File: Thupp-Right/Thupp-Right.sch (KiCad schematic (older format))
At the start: 42 parts

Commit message: aligned footprints relative to plate
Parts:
- MX19: footprint Kailh_Choc:KailhChoc-1U -> Kailh_Choc:KailhChoc-2U
- MX21: footprint Kailh_Choc:KailhChoc-1U -> Kailh_Choc:KailhChoc-1.5U
- MX4: footprint Kailh_Choc:KailhChoc-2U -> Kailh_Choc:KailhChoc-1U
- MX8: footprint Kailh_Choc:KailhChoc-1.5U -> Kailh_Choc:KailhChoc-1U
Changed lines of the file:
@@
 F 0 "MX4" H 2883 1523 60  0000 C CNN
 F 1 "MX-NoLED" H 2883 1449 20  0000 C CNN
-F 2 "Kailh_Choc:KailhChoc-2U" H 2225 1275 60  0001 C CNN
+F 2 "Kailh_Choc:KailhChoc-1U" H 2225 1275 60  0001 C CNN
 F 3 "" H 2225 1275 60  0001 C CNN
 	1    2850 1300
@@
 F 0 "MX8" H 1883 2323 60  0000 C CNN
 F 1 "MX-NoLED" H 1883 2249 20  0000 C CNN
-F 2 "Kailh_Choc:KailhChoc-1.5U" H 1225 2075 60  0001 C CNN
+F 2 "Kailh_Choc:KailhChoc-1U" H 1225 2075 60  0001 C CNN
 F 3 "" H 1225 2075 60  0001 C CNN
 	1    1850 2100
@@
 F 0 "MX19" H 1383 3823 60  0000 C CNN
 F 1 "MX-NoLED" H 1383 3749 20  0000 C CNN
-F 2 "Kailh_Choc:KailhChoc-1U" H 725 3575 60  0001 C CNN
+F 2 "Kailh_Choc:KailhChoc-2U" H 725 3575 60  0001 C CNN
 F 3 "" H 725 3575 60  0001 C CNN
 	1    1350 3600
@@
 F 0 "MX21" H 2383 3823 60  0000 C CNN
 F 1 "MX-NoLED" H 2383 3749 20  0000 C CNN
-F 2 "Kailh_Choc:KailhChoc-1U" H 1725 3575 60  0001 C CNN
+F 2 "Kailh_Choc:KailhChoc-1.5U" H 1725 3575 60  0001 C CNN
 F 3 "" H 1725 3575 60  0001 C CNN
 	1    2350 3600

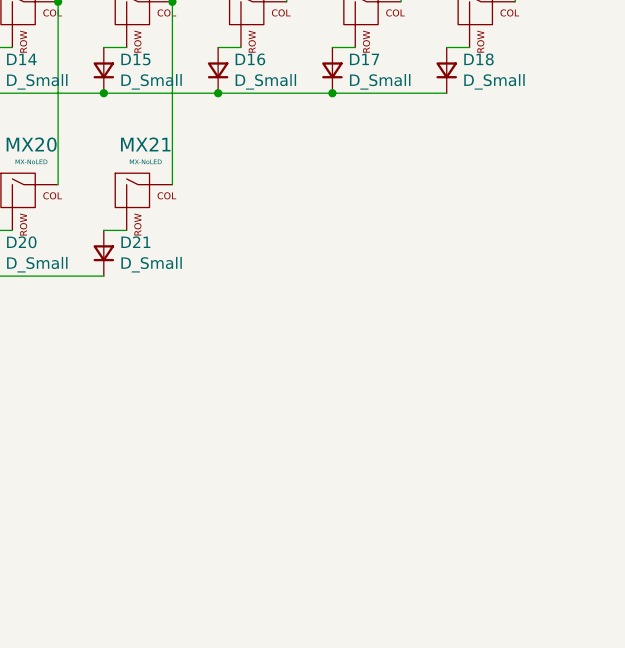
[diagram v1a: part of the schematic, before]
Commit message: adding col assn to nice!nano
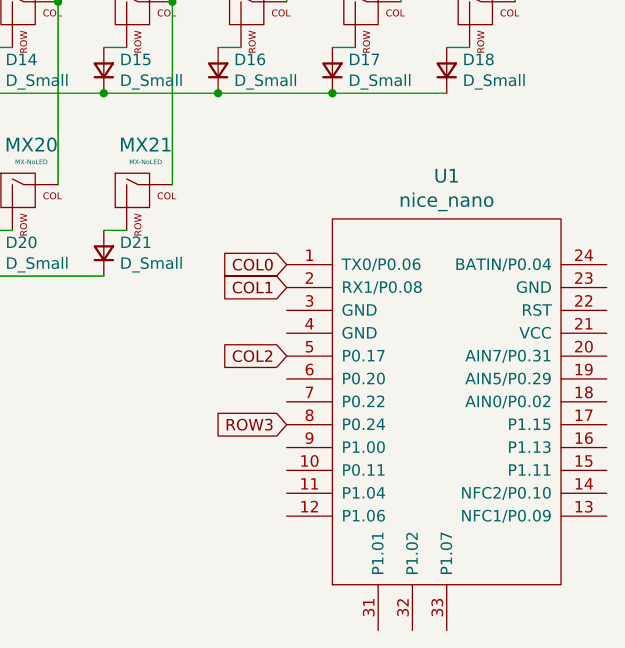
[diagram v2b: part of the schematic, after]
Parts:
- added U1: nice_nano, nice-nano-kicad:nice_nano, symbol nice_nano:nice_nano
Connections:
- net COL0: now also U1.1 (TX0/P0.06)
- net COL1: now also U1.2 (RX1/P0.08)
- net COL2: now also U1.5 (P0.17)
- net ROW3: now also U1.8 (P0.24)
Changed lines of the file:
@@
 Text GLabel 4000 1000 1    50   Input ~ 0
 COL5
+$Comp
+L nice_nano:nice_nano U1
+U 1 1 617DBB1B
+P 3700 4450
+F 0 "U1" H 3700 5387 60  0000 C CNN
+F 1 "nice_nano" H 3700 5281 60  0000 C CNN
+F 2 "nice-nano-kicad:nice_nano" V 4750 1950 60  0001 C CNN
+F 3 "" V 4750 1950 60  0001 C CNN
+	1    3700 4450
+	1    0    0    -1
+$EndComp
+Text GLabel 3000 4600 0    50   Input ~ 0
+ROW3
+Text GLabel 3000 4300 0    50   Input ~ 0
+COL2
+Text GLabel 3000 4000 0    50   Input ~ 0
+COL1
+Text GLabel 3000 3900 0    50   Input ~ 0
+COL0
 $EndSCHEMATC

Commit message: fully routed 1st attempt
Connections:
- net COL3: now also U1.15 (P1.11)
- net COL4: now also U1.17 (P1.15)
- net COL5: now also U1.19 (AIN5/P0.29)
- net ROW0: now also U1.18 (AIN0/P0.02)
- net ROW1: now also U1.16 (P1.13)
- net ROW2: now also U1.14 (NFC2/P0.10)
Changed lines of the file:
@@
 	1300 1450 1200 1450
-$Comp
-L Device:D_Small D1
-U 1 1 6179D221
-P 1200 1550
-F 0 "D1" V 1246 1480 50  0000 R CNN
-F 1 "D_Small" V 1155 1480 50  0000 R CNN
-F 2 "Diode_SMD:D_SOD-123" V 1200 1550 50  0001 C CNN
-F 3 "~" V 1200 1550 50  0001 C CNN
-	1    1200 1550
-	0    -1   -1   0
-$EndComp
 $Comp
 L MX_Alps_Hybrid:MX-NoLED MX2
@@
 Text GLabel 3000 3900 0    50   Input ~ 0
 COL0
+$Comp
+L Device:D_Small D1
+U 1 1 6179D221
+P 1200 1550
+F 0 "D1" V 1246 1480 50  0000 R CNN
+F 1 "D_Small" V 1155 1480 50  0000 R CNN
+F 2 "Diode_SMD:D_SOD-123" V 1200 1550 50  0001 C CNN
+F 3 "~" V 1200 1550 50  0001 C CNN
+	1    1200 1550
+	0    -1   -1   0
+$EndComp
+Text GLabel 4400 4900 2    50   Input ~ 0
+ROW2
+Text GLabel 4400 4800 2    50   Input ~ 0
+COL3
+Text GLabel 4400 4700 2    50   Input ~ 0
+ROW1
+Text GLabel 4400 4600 2    50   Input ~ 0
+COL4
+Text GLabel 4400 4500 2    50   Input ~ 0
+ROW0
+Text GLabel 4400 4400 2    50   Input ~ 0
+COL5
 $EndSCHEMATC
